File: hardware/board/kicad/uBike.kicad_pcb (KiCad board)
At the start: 2 copper layers, 50 x 35 mm, 29 parts, among them J1 KMDGX-6S-BS, J2 F31S-1A7L1-11040, J3 KMDGX-8S-BS, J4 FTSH-105-01-F-DV-K, Q1 MMBT3904, U1 SN65HVD08DR, U2 LD1117S33TR_SOT223, U3 MDBT50Q-P1MV2, X1 32.768kHz

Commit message: Roughed in
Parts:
- added C10: 100nF, Capacitor_SMD:C_0805_2012Metric, F.Cu at (82.0, 47.8)
- added C11: 22pF, Capacitor_SMD:C_0603_1608Metric, F.Cu at (66.4, 62.0)
- added C12: 33uF, Capacitor_SMD:C_1206_3216Metric, F.Cu at (58.2, 68.1)
- added C13: 2u2, Capacitor_SMD:C_0603_1608Metric, F.Cu at (71.1, 40.5)
- added C14: 2u2, Capacitor_SMD:C_0603_1608Metric, F.Cu at (60.6, 56.1)
- added C7: 100nF, Capacitor_SMD:C_0805_2012Metric, F.Cu at (60.3, 53.8)
- added C8: 10uF, Capacitor_SMD:C_1206_3216Metric, F.Cu at (76.5, 73.9)
- added C9: 10nF, Capacitor_SMD:C_0805_2012Metric, F.Cu at (66.4, 68.3)
- added D1: CDSOT23-SM712, libs:SOT95P230X117-3N, F.Cu at (75.0, 44.9)
- added D2: GREEN, Diode_SMD:D_1206_3216Metric, F.Cu at (103.0, 88.0)
- added D3: RED, Diode_SMD:D_1206_3216Metric, F.Cu at (58.2, 71.1)
- added D4: CDSOT23-SM712, libs:SOT95P230X117-3N, F.Cu at (95.1, 41.1)
- added D6: CDSOT23-SM712, libs:SOT95P230X117-3N, F.Cu at (100.8, 41.1)
- added F1: 2A, Diode_SMD:D_1206_3216Metric, F.Cu at (65.5, 74.5)
- added H4: MountingHole, MountingHole:MountingHole_3.2mm_M3, F.Cu at (60.0, 30.0)
- added J5: 87520-0010BLF, libs:87520-0010BLF, F.Cu at (64.4, 82.5)
- added L1: 120, libs:L_Bourns_5050, F.Cu at (63.0, 45.7)
- added R12: 10k, Resistor_SMD:R_0603_1608Metric, F.Cu at (66.4, 66.0)
- added R13: 120, Resistor_SMD:R_0603_1608Metric, F.Cu at (78.7, 43.2)
- added R14: 10, Resistor_SMD:R_0603_1608Metric, F.Cu at (73.7, 40.5)
- added R15: 10, Resistor_SMD:R_0603_1608Metric, F.Cu at (76.2, 40.5)
- added R16: 220k, Resistor_SMD:R_0603_1608Metric, F.Cu at (66.4, 60.0)
- added R17: 30k, Resistor_SMD:R_0603_1608Metric, F.Cu at (66.4, 64.0)
- added R18: 150, Resistor_SMD:R_0805_2012Metric, F.Cu at (58.2, 73.9)
- added R19: 157, Resistor_SMD:R_0603_1608Metric, F.Cu at (68.0, 86.0)
- added R20: 68, Resistor_SMD:R_0805_2012Metric, F.Cu at (107.4, 88.1)
- added U4: PTPSM863252RDXR, libs:TPSM863252RDX, F.Cu at (59.7, 60.0)
- C2: value 100nF -> 10uF; footprint Capacitor_SMD:C_0805_2012Metric -> Capacitor_SMD:C_1206_3216Metric
- C3: value 10uF -> 100nF; footprint Capacitor_SMD:C_1206_3216Metric -> Capacitor_SMD:C_0805_2012Metric
- H1, H2, H3: footprint MountingHole:MountingHole_2.7mm_M2.5 -> MountingHole:MountingHole_3.2mm_M3
- J1: footprint KMDGX-6S-BS:KMDGX6SBS -> libs:KMDGX6SBS
- J2: footprint F31S-1A7L1-11040:F31S1A7L111040 -> libs:F31S1A7L111040
- J3: footprint KMDGX-8S-BS:KMDGX8SBS -> libs:KMDGX8SBS
- J4: value FTSH-105-01-F-DV-K -> TC2050-IDC-NL; footprint FTSH-105-01-F-DV-K:FTSH10501FDVK -> Connector:Tag-Connect_TC2050-IDC-NL_2x05_P1.27mm_Vertical
- R1, R2, R3, R6, R7, R8: value 390 -> 68
- R5: value 120 -> 61.9k
- U1: footprint SN65HVD08DR:SOIC127P600X175-8N -> libs:SOIC127P600X175-8N
- moved R11 97.5 mm to (70.0, 128.5), turned to 0 degrees
- moved Q1 94.5 mm to (73.6, 127.6), turned to 90 degrees
- moved R6 87.4 mm to (69.2, 123.2), turned to -90 degrees
- moved R1 86.5 mm to (71.4, 123.2), turned to 90 degrees
- moved R2 85.8 mm to (73.6, 123.2), turned to 90 degrees
- moved R3 85.3 mm to (75.8, 123.2), turned to 90 degrees
- moved R7 85.0 mm to (78.0, 123.2), turned to -90 degrees
- moved R8 78.2 mm to (80.2, 119.8), turned to -90 degrees
- moved J2 58.9 mm to (76.8, 100.0), turned to 0 degrees
- moved H3 57.6 mm to (60.0, 100.0)
- moved H2 49.7 mm to (110.0, 100.0)
- moved J4 49.5 mm to (105.9, 81.5)
- moved C3 28.0 mm to (71.7, 73.9), turned to 0 degrees
- moved R9 25.9 mm to (106.2, 65.0)
- moved U2 25.4 mm to (74.3, 68.7), turned to 0 degrees
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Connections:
- net Net-(J4-Pad2) renamed SWDIO
- net Net-(J4-Pad4) renamed SWCLK
- net XL renamed CTP_SCL
- net XR renamed CTP_SDA
- C1 pad 1: GND -> +3.3V
- C1 pad 2: +3.3V -> GND
- C3 pad 1: +3.3V -> +5V
- J2 pad 33: +12V -> +5V
- J3 pad 1: +12V -> 12_VIN
- J3 pad 7: +12V -> 12_VIN
- J4 pad 9: GND -> unconnected-(J4-Pad9)
- R5 pad 1: Net-(J3-Pad3) -> Net-(U4-EN)
- R5 pad 2: Net-(J3-Pad4) -> +12V
- U1 pad 6: Net-(J3-Pad4) -> RS485_A
- U1 pad 7: Net-(J3-Pad3) -> RS485_B
- U2 pad 3: +12V -> +5V
- U3 pad 37: unconnected-(U3-Pad37) -> Net-(D2-A)
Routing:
- net SWO: track 49.5 -> 0.00 mm, vias 2 -> 0
- net SWCLK: track 48.0 -> 0.00 mm, vias 2 -> 0
- net SWDIO: track 47.5 -> 0.00 mm
- net SWD_RST: track 42.7 -> 0.00 mm, vias 2 -> 0
- net Net-(U4-EN): track 0.00 -> 31.3 mm, vias 0 -> 2
- net +12V: track 27.8 -> 0.00 mm, vias 1 -> 0
- net BL_PWM: track 23.9 -> 0.00 mm, vias 2 -> 0
- net Net-(J3-Pad3): track 32.5 -> 14.7 mm
- net YU: track 17.5 -> 0.00 mm, vias 2 -> 0
- net IN3: track 26.5 -> 10.1 mm, vias 1 -> 0
- net RX: track 20.4 -> 4.60 mm, vias 2 -> 0
- net SDO: track 15.2 -> 0.00 mm, vias 2 -> 0
- net IN1: track 25.1 -> 10.4 mm, vias 1 -> 0
- net Net-(J3-Pad4): track 22.8 -> 8.51 mm
- net IN4: track 22.3 -> 8.18 mm, vias 1 -> 0
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- added copper zone on F.Cu, net +5V
- added copper zone on F.Cu, net 12_VIN
- added copper zone on In1.Cu, net GND
- added copper zone on F.Cu, net Net-(F1-Pad2)
- removed copper zone on F.Cu, net BL_DRAIN
- removed copper zone on B.Cu, net GND
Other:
- board size 50 x 35 mm -> 60 x 80 mm
- copper layers 2 -> 4
- board text added: "C13"
- board text added: "Greco Engineering Solutions LLC"
- board text added: "uBike v0.4"
- board text removed: "uBike v0.3"

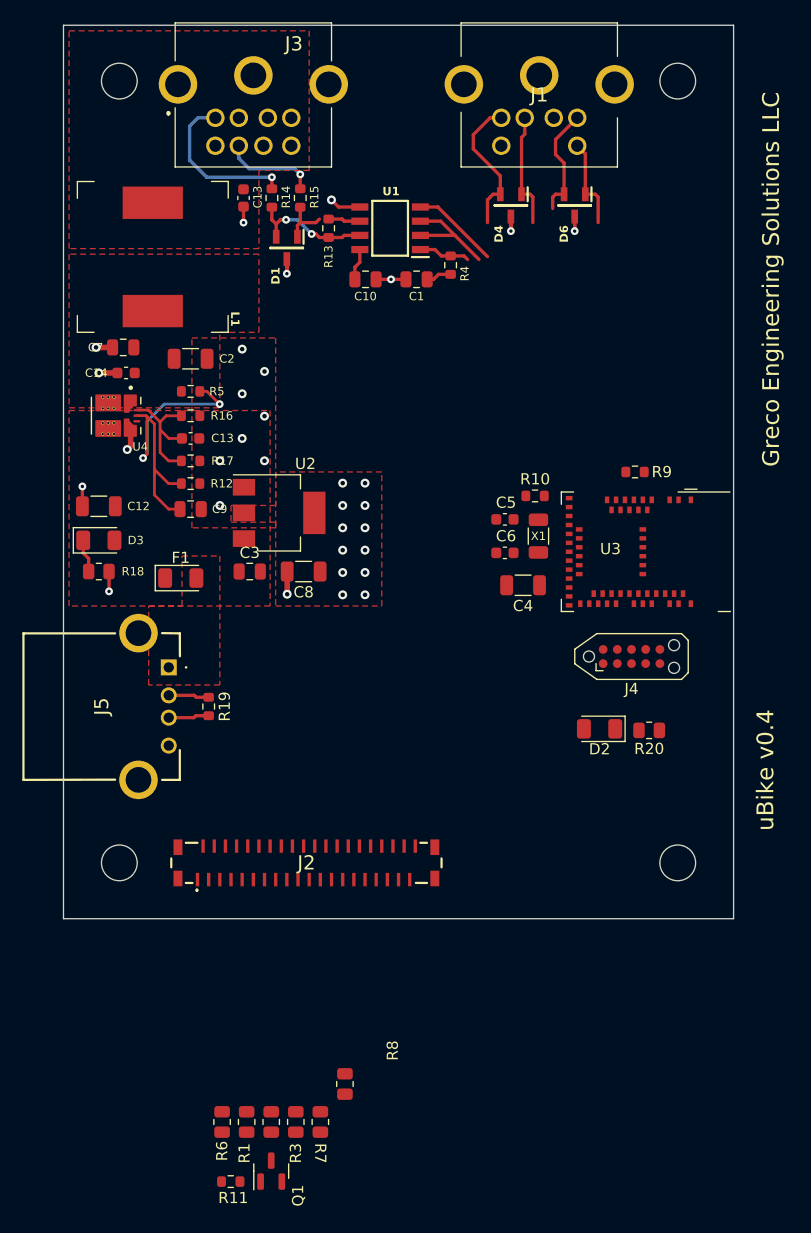
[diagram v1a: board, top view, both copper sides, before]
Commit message: Changed to 2-layer board
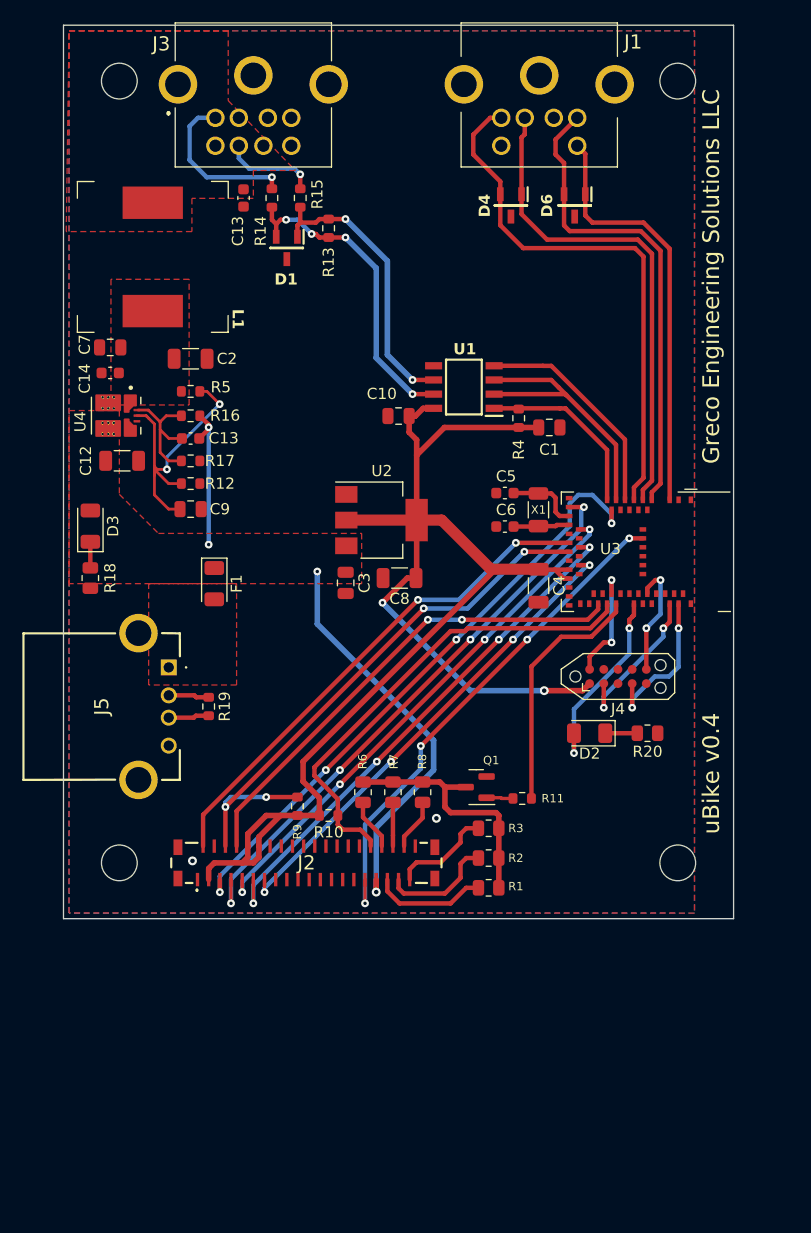
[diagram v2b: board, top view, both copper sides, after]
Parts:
- moved R11 43.1 mm to (96.1, 94.2), turned to 180 degrees
- moved R9 42.5 mm to (75.9, 94.9), turned to 90 degrees
- moved Q1 39.0 mm to (91.9, 93.2), turned to 180 degrees
- moved R10 34.1 mm to (78.7, 95.8), turned to 0 degrees
- moved R6 32.1 mm to (81.8, 93.7), turned to 90 degrees
- moved R3 31.5 mm to (93.1, 96.9), turned to 180 degrees
- moved R2 30.6 mm to (93.1, 99.6), turned to 180 degrees
- moved R7 30.2 mm to (84.5, 93.7), turned to 90 degrees
- moved R1 30.1 mm to (93.1, 102.2), turned to 180 degrees
- moved R8 27.0 mm to (87.2, 93.7), turned to 90 degrees
- moved C1 17.8 mm to (98.5, 61.0), turned to 0 degrees
- moved U1 15.7 mm to (90.8, 57.4)
- moved R4 15.0 mm to (95.8, 60.2)
- moved C10 12.6 mm to (85.0, 60.0), turned to 0 degrees
- moved U2 9.18 mm to (83.5, 69.3)
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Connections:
- U3 pad 10: RS -> TX
- U3 pad 12: CS -> DE
- U3 pad 13: SDO -> YD
- U3 pad 14: SCL -> RX
- U3 pad 16: CTP_SDA -> RESET
- U3 pad 19: BL_PWM -> CS
- U3 pad 22: unconnected-(U3-P0.06-Pad22) -> SDI
- U3 pad 23: YU -> SCL
- U3 pad 24: unconnected-(U3-P0.08-Pad24) -> CTP_SCL
- U3 pad 25: TX -> unconnected-(U3-P1.08-Pad25)
- U3 pad 27: DE -> SDO
- U3 pad 29: RX -> unconnected-(U3-TRACEDATA1/P0.12-Pad29)
- U3 pad 3: SDI -> IN4
- U3 pad 37: Net-(D2-A) -> RS
- U3 pad 39: unconnected-(U3-P0.15-Pad39) -> CTP_SDA
- U3 pad 4: YD -> IN3
- U3 pad 41: unconnected-(U3-P0.17-Pad41) -> BL_PWM
- U3 pad 44: unconnected-(U3-P0.20-Pad44) -> Net-(D2-A)
- U3 pad 57: unconnected-(U3-P1.06-Pad57) -> YU
- U3 pad 58: IN2 -> unconnected-(U3-P1.07-Pad58)
- U3 pad 59: IN1 -> unconnected-(U3-P1.05-Pad59)
- U3 pad 6: CTP_SCL -> IN1
- U3 pad 60: IN4 -> unconnected-(U3-P1.03-Pad60)
- U3 pad 61: IN3 -> unconnected-(U3-P1.01-Pad61)
- U3 pad 8: RESET -> IN2
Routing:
- net +3.3V: track 5.13 -> 132.7 mm, vias 12 -> 2
- net YD: track 0.00 -> 55.7 mm, vias 0 -> 4
- net RESET: track 0.00 -> 52.0 mm, vias 0 -> 4
- net CTP_SCL: track 0.00 -> 50.8 mm, vias 0 -> 4
- net +5V: track 0.00 -> 49.5 mm, vias 0 -> 4
- net CS: track 0.00 -> 47.4 mm, vias 0 -> 4
- net SCL: track 0.00 -> 47.4 mm, vias 0 -> 4
- net YU: track 0.00 -> 46.3 mm, vias 0 -> 4
- net SDI: track 0.00 -> 45.7 mm, vias 0 -> 2
- net SDO: track 0.00 -> 43.5 mm, vias 0 -> 4
- net RS: track 0.00 -> 43.5 mm, vias 0 -> 2
- net CTP_SDA: track 0.00 -> 42.9 mm
- net IN2: track 12.9 -> 48.4 mm
- net IN1: track 10.4 -> 44.3 mm
- net IN3: track 10.1 -> 43.0 mm
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- added copper zone on B.Cu, net GND
- removed copper zone on F.Cu, net +3.3V
- removed copper zone on In1.Cu, net GND
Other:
- copper layers 4 -> 2
- board text added: "R2"
